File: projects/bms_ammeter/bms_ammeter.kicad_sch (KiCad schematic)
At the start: 9 parts, among them IC1 ADS1246IPWR, U2 AP7370-12FDC, U3 ADUM4150ARIZ-RL

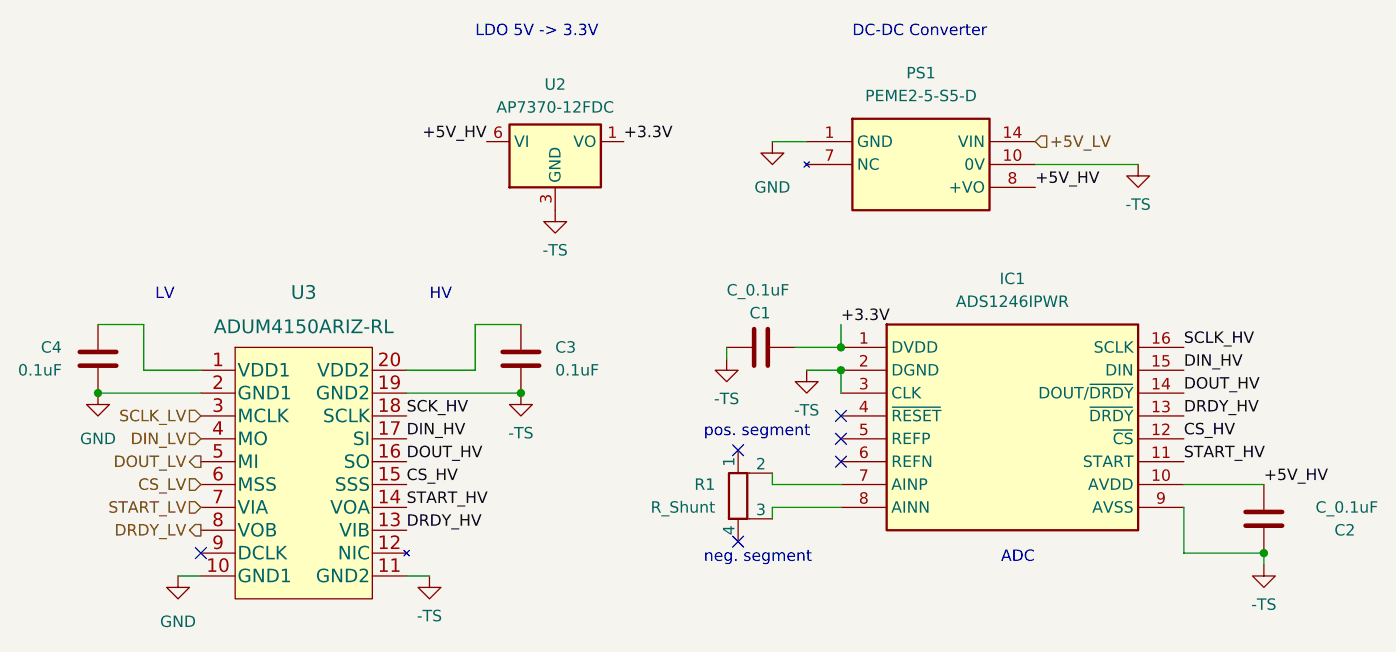
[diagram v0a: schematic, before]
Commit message: Added revisions from Melissa's comments
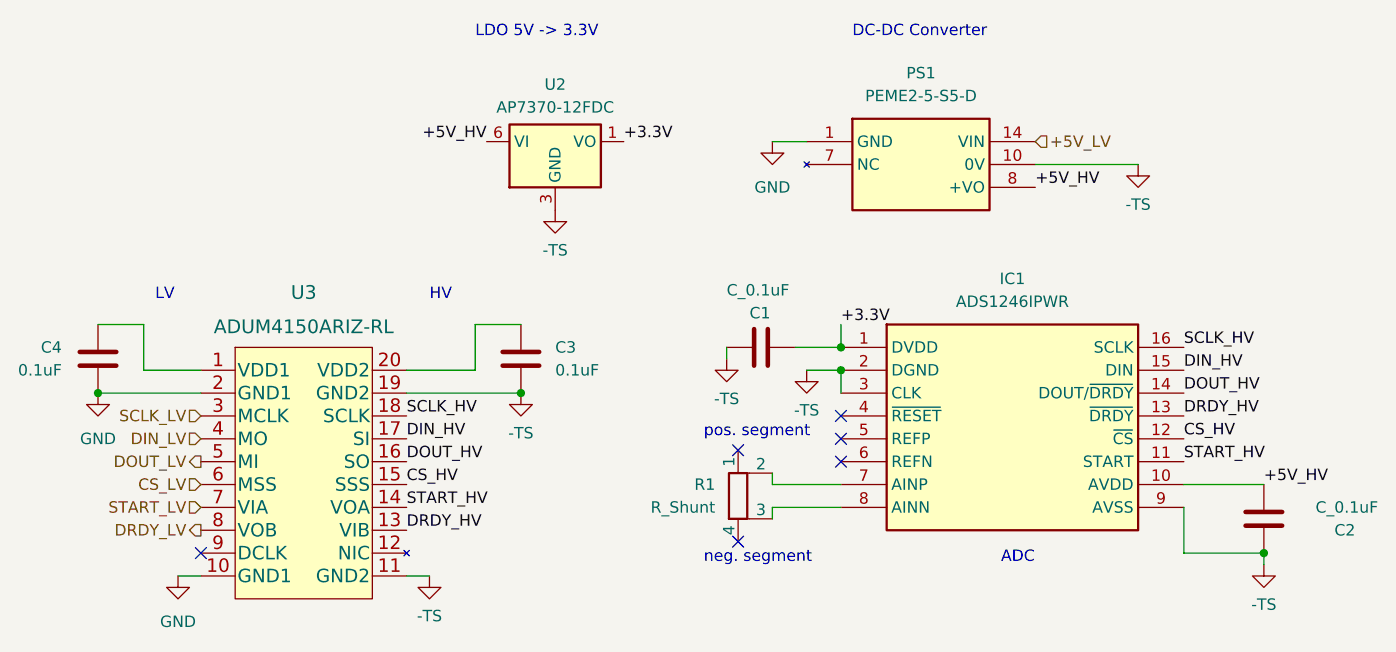
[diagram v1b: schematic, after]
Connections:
- net SCK_HV is gone; now on net SCLK_HV: U3.18 (SCLK)
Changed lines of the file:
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@@
     (effects (font (size 1.27 1.27)) (justify left bottom))
   )
-  (label "SCK_HV" (at 105.41 91.44 0) (fields_autoplaced)
+  (label "SCLK_HV" (at 105.41 91.44 0) (fields_autoplaced)
     (effects (font (size 1.27 1.27)) (justify left bottom))
   )
@@
     )
   )
+  (sheet_instances
+    (path "/" (page "1"))
+  )
 )
